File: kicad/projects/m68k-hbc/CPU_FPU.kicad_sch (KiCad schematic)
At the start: 19 parts, among them IC1 MC68030RC, IC2 MC68881FN

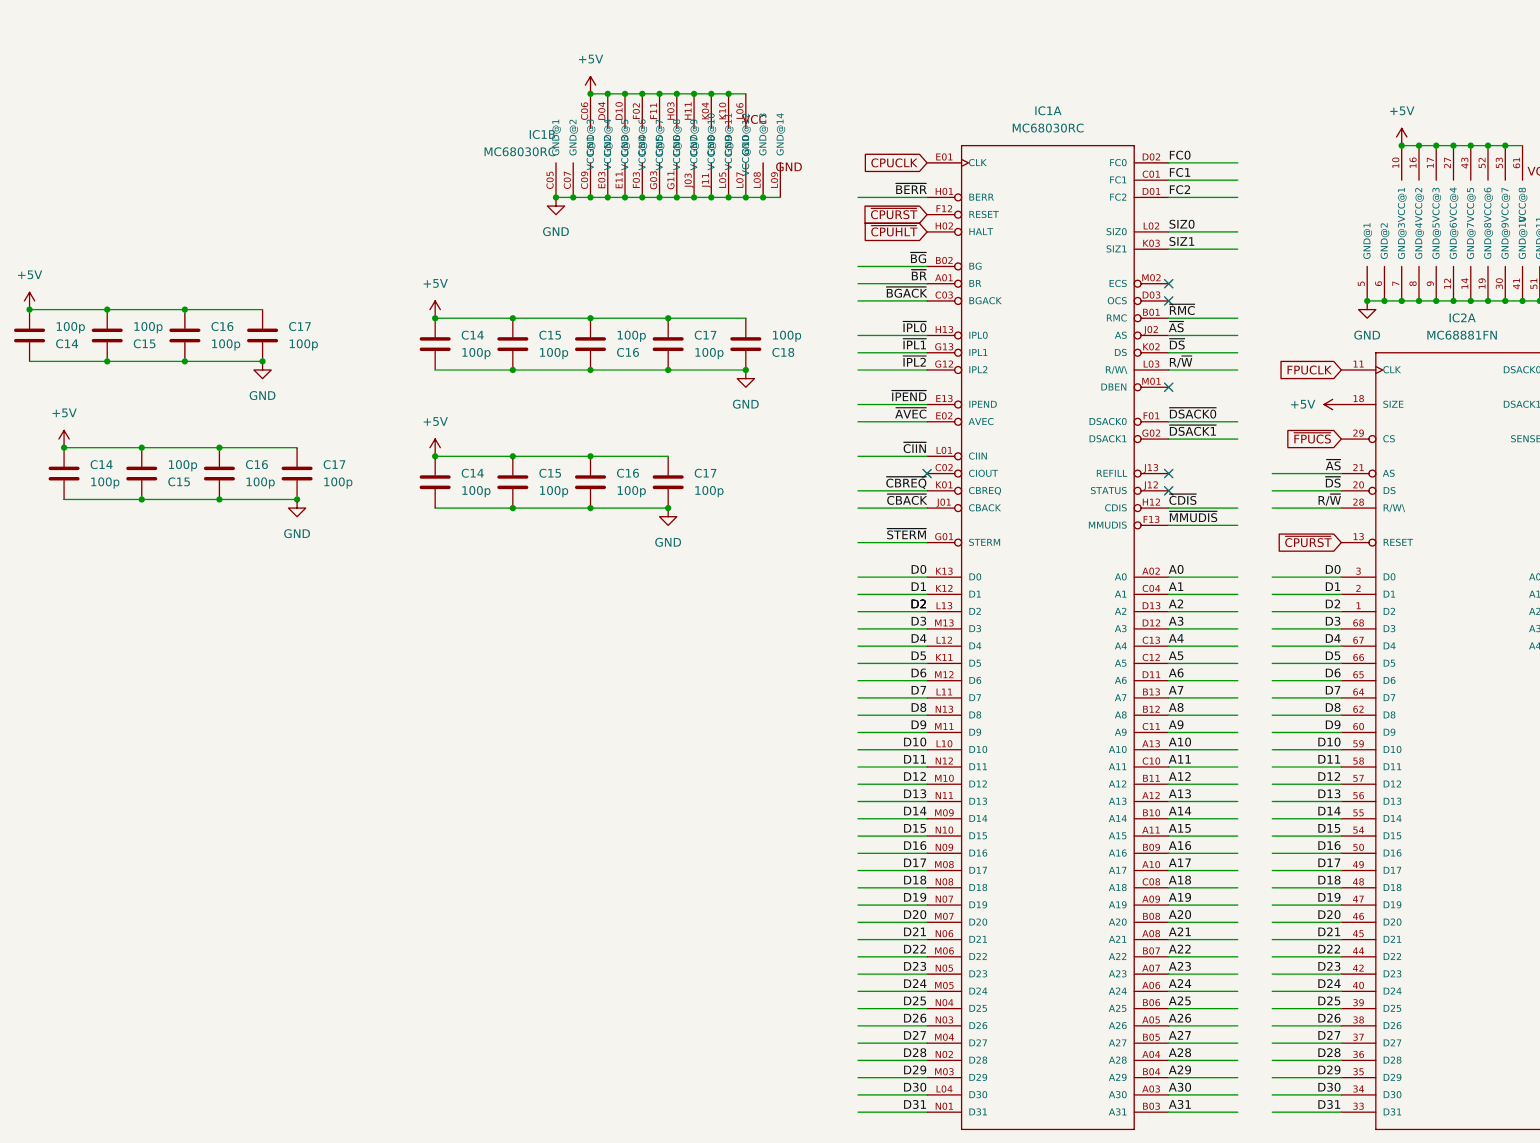
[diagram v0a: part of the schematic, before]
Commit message: Modified system architecture, New KiCad Project: Cache Memory Module(SIMM80)
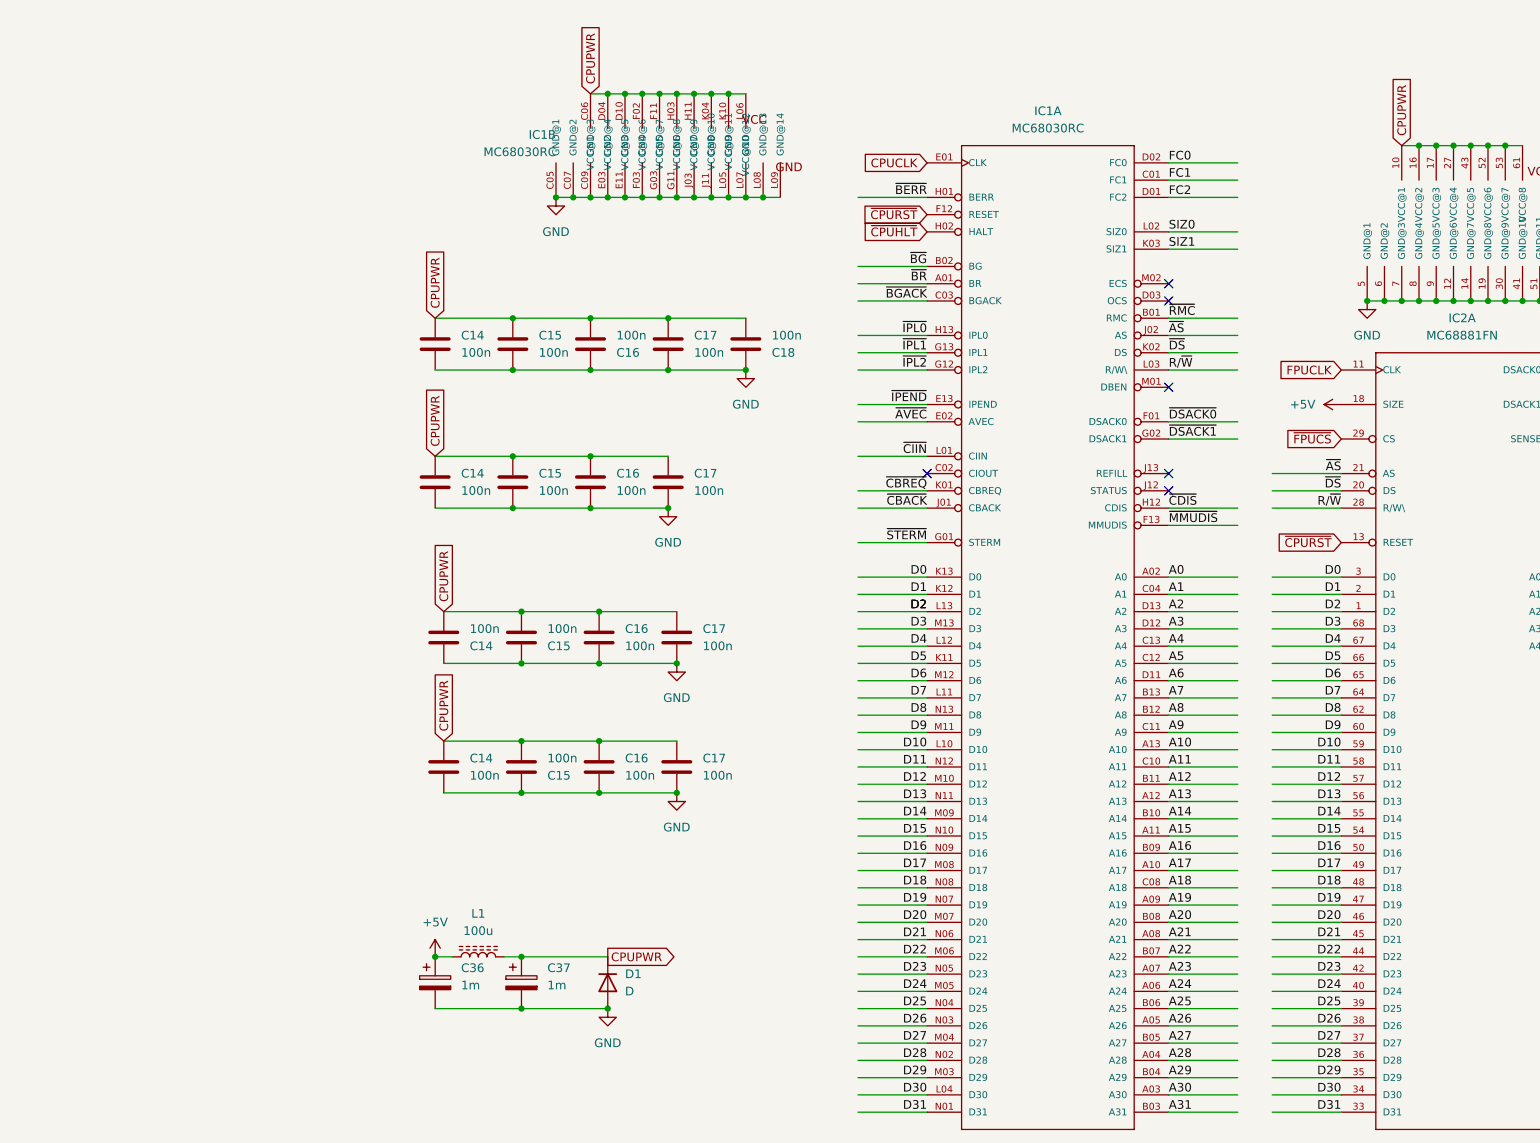
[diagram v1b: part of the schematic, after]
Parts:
- added C36, C37: 1m, Capacitor_THT:CP_Radial_D8.0mm_P3.50mm, symbol Device:C_Polarized
- added D1: D, Diode_THT:D_5W_P10.16mm_Horizontal, symbol Device:D
- added L1: 100u, Inductor_THT:L_Toroid_Vertical_L13.0mm_W6.5mm_P5.60mm, symbol Device:L_Ferrite
- C14, C15, C16, C17, C18: value 100p -> 100n
- IC1: footprint PGA68:PGA128 -> m68k-hbc-ic:PGA128
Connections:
- net +5V: now also C36.1, L1.1; no longer C14.1, C14.1, C14.1, C14.2, C15.1, C15.1, C15.2, C15.2, C16.1, C16.1, C16.1, C16.2, C17.1, C17.1, C17.1, C17.1, C18.2, IC1.C06 (VCC@1), IC1.D04 (VCC@2), IC1.D10 (VCC@3), IC1.F02 (VCC@4), IC1.F11 (VCC@5), IC1.H03 (VCC@6), IC1.H11 (VCC@7), IC1.K04 (VCC@8), IC1.K10 (VCC@9), IC1.L06 (VCC@10), IC2.10 (VCC@1), IC2.16 (VCC@2), IC2.17 (VCC@3), IC2.27 (VCC@4), IC2.43 (VCC@5), IC2.52 (VCC@6), IC2.53 (VCC@7), IC2.61 (VCC@8)
- net GND: now also C36.2, C37.2, D1.2 (A)
- new net CPUPWR: C14.1, C14.1, C14.1, C14.2, C15.1, C15.1, C15.2, C15.2, C16.1, C16.1, C16.1, C16.2, C17.1, C17.1, C17.1, C17.1, C18.2, C37.1, D1.1 (K), IC1.C06 (VCC@1), IC1.D04 (VCC@2), IC1.D10 (VCC@3), IC1.F02 (VCC@4), IC1.F11 (VCC@5), IC1.H03 (VCC@6), IC1.H11 (VCC@7), IC1.K04 (VCC@8), IC1.K10 (VCC@9), IC1.L06 (VCC@10), IC2.10 (VCC@1), IC2.16 (VCC@2), IC2.17 (VCC@3), IC2.27 (VCC@4), IC2.43 (VCC@5), IC2.52 (VCC@6), IC2.53 (VCC@7), IC2.61 (VCC@8), L1.2
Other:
- moved on the sheet: C14, C15, C16, C17

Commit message: Some Updates
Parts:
- removed C36, C37: 1m, Capacitor_THT:CP_Radial_D8.0mm_P3.50mm, symbol Device:C_Polarized
- removed D1: D, Diode_THT:D_5W_P10.16mm_Horizontal, symbol Device:D
- removed L1: 100u, Inductor_THT:L_Toroid_Vertical_L13.0mm_W6.5mm_P5.60mm, symbol Device:L_Ferrite
- added R1: R, Resistor_SMD:R_0603_1608Metric_Pad0.98x0.95mm_HandSolder, symbol Device:R
- C14, C15, C16, C17, C18: value 100n -> C; footprint Capacitor_SMD:C_1206_3216Metric_Pad1.33x1.80mm_HandSolder -> Capacitor_SMD:C_0603_1608Metric_Pad1.08x0.95mm_HandSolder
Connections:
- net +5V: now also R1.1
- net ~{CIOUT}: now reaches IC1.C02 (CIOUT)
- net ~{PRES_FPU}: now reaches IC2.4 (SENSE)
- net ~{PRES_FPU}: now also R1.2
- net CPUPWR renamed PWR_CPURAM
- net ~{CPUHLT} renamed ~{HLT_CPU}
- net ~{CPURST} renamed ~{RST_CPU}
- net ~{RST_CPU}: no longer IC2.13 (RESET)
- net ~{FPUCS} renamed ~{CS_FPU}
- new net ~{RST_FPU}: IC2.13 (RESET)
- no-connect marks 7 -> 5
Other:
- note added: "Local Bus Signals"
- moved on the sheet: C14, C15, C16, C17, C18, IC1A, IC1B, IC2A, IC2B
